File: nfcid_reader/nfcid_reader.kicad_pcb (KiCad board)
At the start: 2 copper layers, 20 parts, among them J1 BARREL_JACK, J2 ESP32_LEFT, J3 ESP32_RIGHT, J4 PN532, Q1 Q_PMOS_GSD, U1 MCP73832-2-OT, U2 LF33_TO220

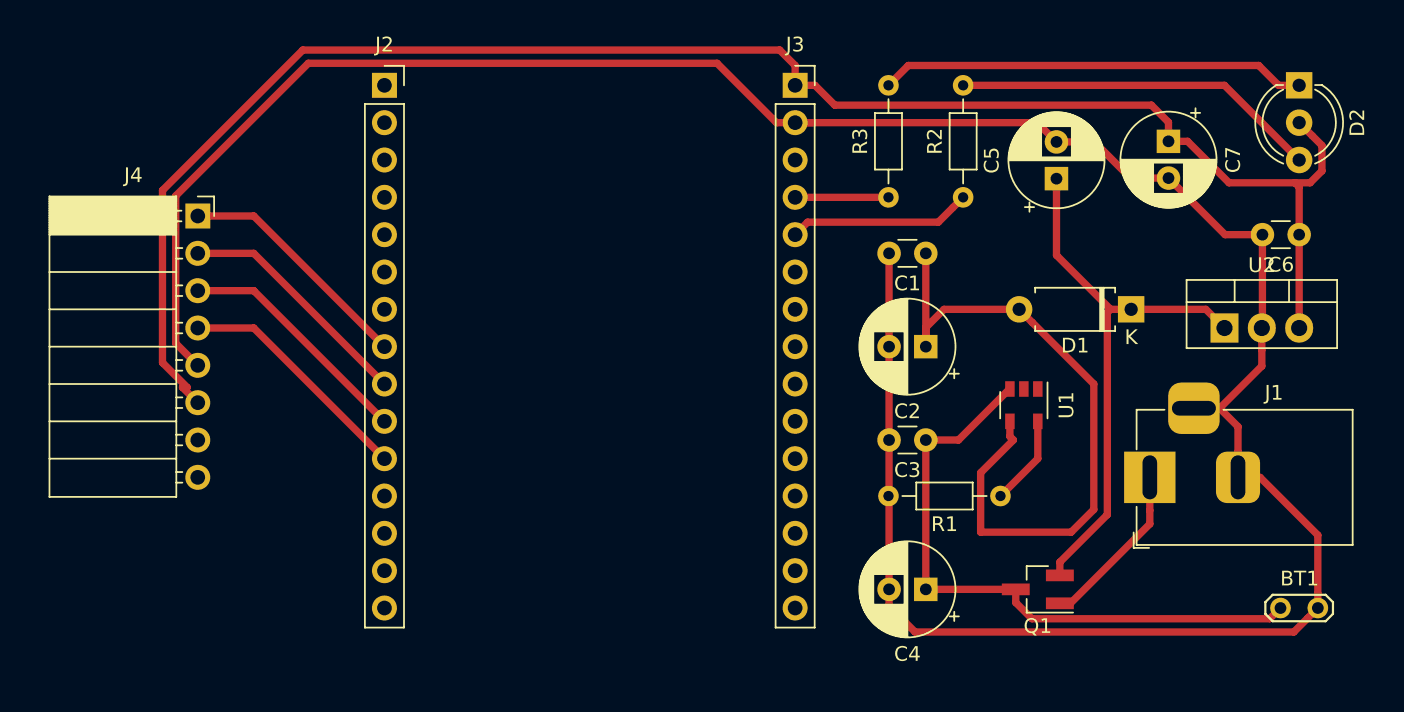
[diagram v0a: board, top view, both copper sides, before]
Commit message: Fixed thick track, ESP orentation. Added bridge, edge cuts.
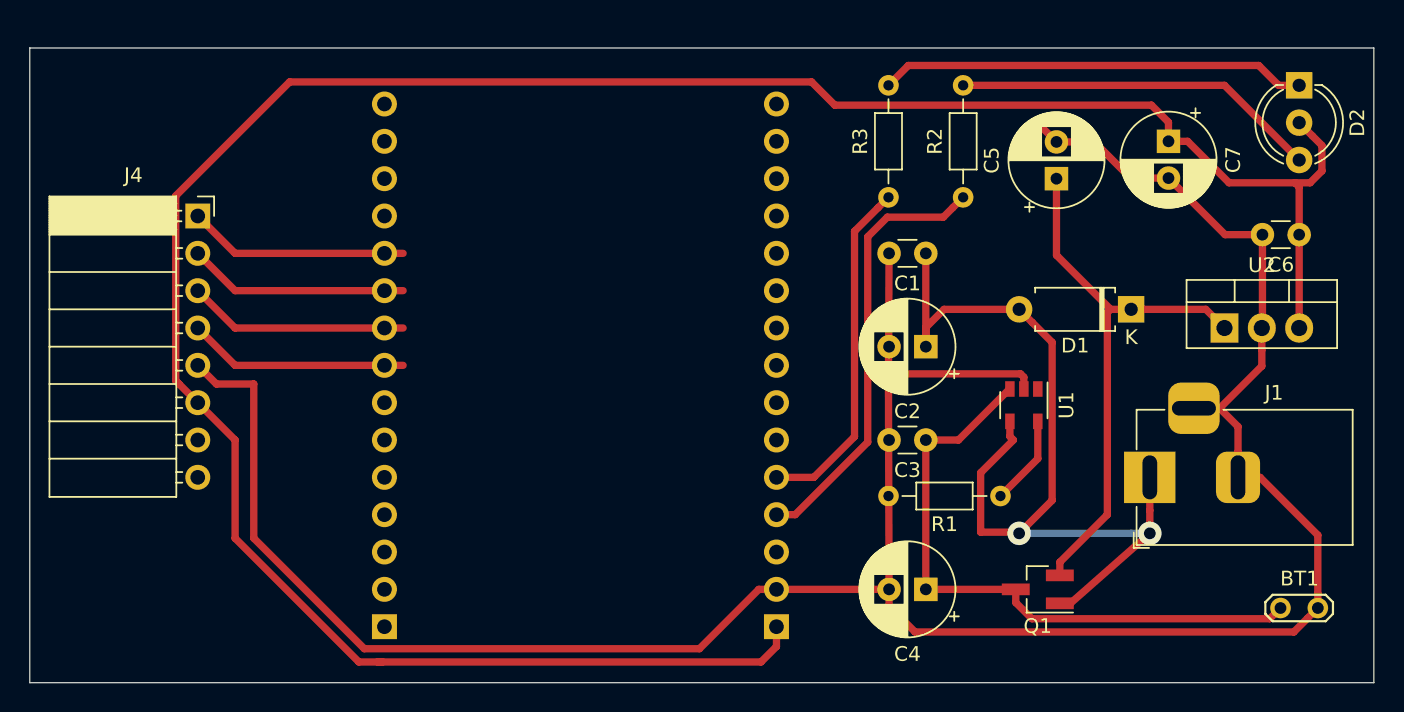
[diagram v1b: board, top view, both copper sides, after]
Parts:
- J2, J3: moved to B.Cu
- moved J3 36.9 mm to (81.3, 124.5)
- moved J2 36.8 mm to (54.6, 124.5)
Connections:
- J2 pad 10: SPI_MOSI -> SPI_MISO
- J2 pad 11: SPI_SS -> SPI_SCK
- J2 pad 8: SPI_SCK -> SPI_SS
- J2 pad 9: SPI_MISO -> SPI_MOSI
- R2 pad 1: Net-(J3-Pad5) -> Net-(J3-Pad4)
- R3 pad 1: Net-(J3-Pad4) -> Net-(J3-Pad5)
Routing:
- net +3V3: track 118.3 -> 166.4 mm
- net Net-(J3-Pad4): track 6.35 -> 29.8 mm
- net Net-(J3-Pad5): track 12.5 -> 23.7 mm
- net +5V: track 58.7 -> 63.4 mm, vias 0 -> 2
- net GND: track 182.4 -> 178.3 mm
- net SPI_MISO: track 16.4 -> 15.0 mm
- net SPI_SS: track 16.4 -> 15.0 mm
- net SPI_SCK: track 16.4 -> 15.0 mm
- net SPI_MOSI: track 16.4 -> 15.0 mm
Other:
- board outline added: 91.4 x 43.2 mm
- net class Default: clearance 0.4 -> 0.25
- rule trace_clearance: 0.4 -> 0.25

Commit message: Minor fixes.
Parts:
- J2, J3: moved to F.Cu
- moved BT1 10.6 mm to (105.0, 124.5)
- turned J2 to 180 degrees
- turned J3 to 180 degrees
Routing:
- net Net-(BT1-Pad1): track 43.1 -> 32.4 mm
- net GND: track 178.3 -> 169.1 mm
- net SPI_SS: track 15.0 -> 13.8 mm
- net SPI_SCK: track 15.0 -> 13.8 mm
- net SPI_MOSI: track 15.0 -> 13.8 mm
- net SPI_MISO: track 15.0 -> 13.8 mm
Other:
- board size 91.4 x 43.2 mm -> 83.8 x 43.2 mm
- net class Default: clearance 0.25 -> 0.4
- rule trace_clearance: 0.25 -> 0.4

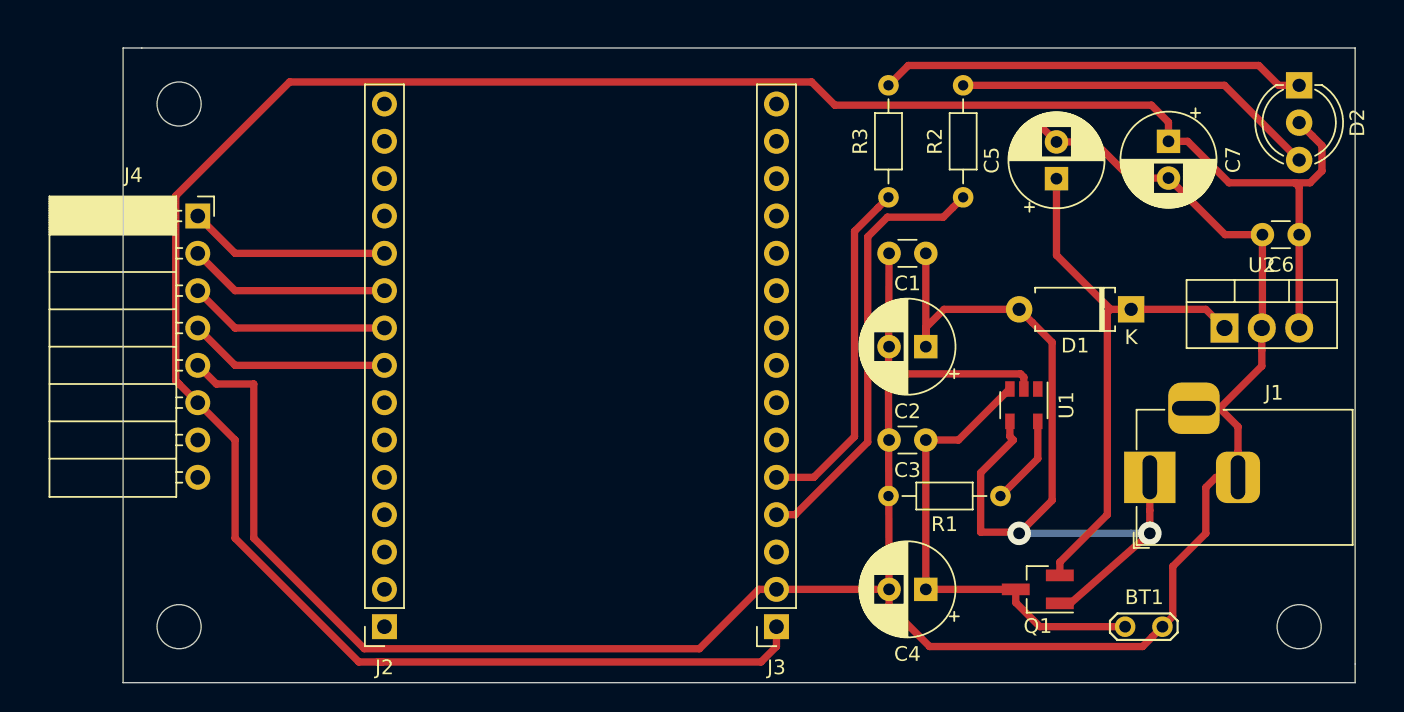
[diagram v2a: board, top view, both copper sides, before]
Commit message: RC-1: Added votage dividers. J4 fliped.
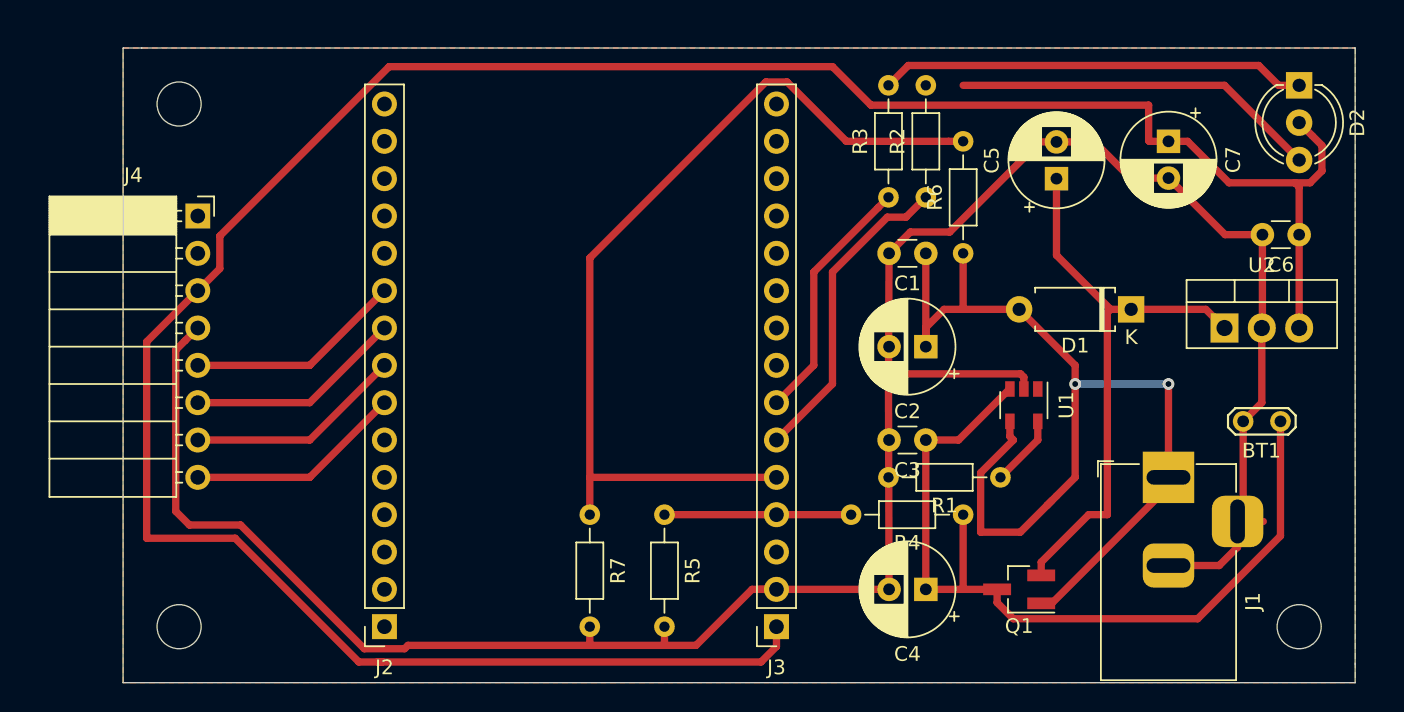
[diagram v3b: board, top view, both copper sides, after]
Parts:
- added R4: 4K7, Resistor_THT:R_Axial_DIN0204_L3.6mm_D1.6mm_P7.62mm_Horizontal, F.Cu at (94.0, 116.8)
- added R5: 1K, Resistor_THT:R_Axial_DIN0204_L3.6mm_D1.6mm_P7.62mm_Horizontal, F.Cu at (73.7, 116.8)
- added R6: 4K7, Resistor_THT:R_Axial_DIN0204_L3.6mm_D1.6mm_P7.62mm_Horizontal, F.Cu at (94.0, 99.1)
- added R7: 4K7, Resistor_THT:R_Axial_DIN0204_L3.6mm_D1.6mm_P7.62mm_Horizontal, F.Cu at (68.6, 116.8)
- moved BT1 17.5 mm to (115.6, 110.5), turned to 180 degrees
- moved R2 2.54 mm to (91.4, 95.2)
- moved J1 1.27 mm to (108.0, 114.3), turned to 90 degrees
- moved Q1 1.27 mm to (97.8, 121.9)
- moved R1 1.27 mm to (96.5, 114.3)
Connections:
- J2 pad 10: SPI_MISO -> SPI_SS
- J2 pad 11: SPI_SCK -> Net-(J2-Pad11)
- J2 pad 7: Net-(J2-Pad7) -> SPI_SCK
- J2 pad 8: SPI_SS -> SPI_MISO
- J3 pad 4: Net-(J3-Pad4) -> POW_BATT
- J3 pad 5: Net-(J3-Pad5) -> POW_SOUR
- J4 pad 1: SPI_SCK -> Net-(J4-Pad1)
- J4 pad 2: SPI_MISO -> Net-(J4-Pad2)
- J4 pad 3: SPI_MOSI -> +3V3
- J4 pad 4: SPI_SS -> GND
- J4 pad 5: GND -> SPI_SS
- J4 pad 6: +3V3 -> SPI_MOSI
- J4 pad 7: Net-(J4-Pad7) -> SPI_MISO
- J4 pad 8: Net-(J4-Pad8) -> SPI_SCK
- R2 pad 1: Net-(J3-Pad4) -> Net-(J3-Pad6)
- R3 pad 1: Net-(J3-Pad5) -> Net-(J3-Pad7)
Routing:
- net POW_SOUR: track 0.00 -> 62.2 mm
- net Net-(J3-Pad4): track 29.8 -> 0.00 mm
- net Net-(BT1-Pad1): track 32.4 -> 58.0 mm
- net Net-(J3-Pad5): track 23.7 -> 0.00 mm
- net Net-(J3-Pad6): track 0.00 -> 21.5 mm
- net Net-(J3-Pad7): track 0.00 -> 17.1 mm
- net POW_BATT: track 0.00 -> 12.7 mm
- net +5V: track 63.4 -> 73.6 mm
- net GND: track 169.1 -> 164.2 mm
- net +3V3: track 166.4 -> 169.8 mm
- net VCC: track 38.2 -> 39.5 mm
- net Net-(R1-Pad1): track 6.13 -> 4.86 mm
- net SPI_SS: track 13.8 -> 14.8 mm
- net SPI_MISO: track 13.8 -> 14.8 mm
- net SPI_SCK: track 13.8 -> 14.8 mm
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- added copper zone on F.Cu, net GND

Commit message: RC-2: U2 changed to SMD. LED moved.
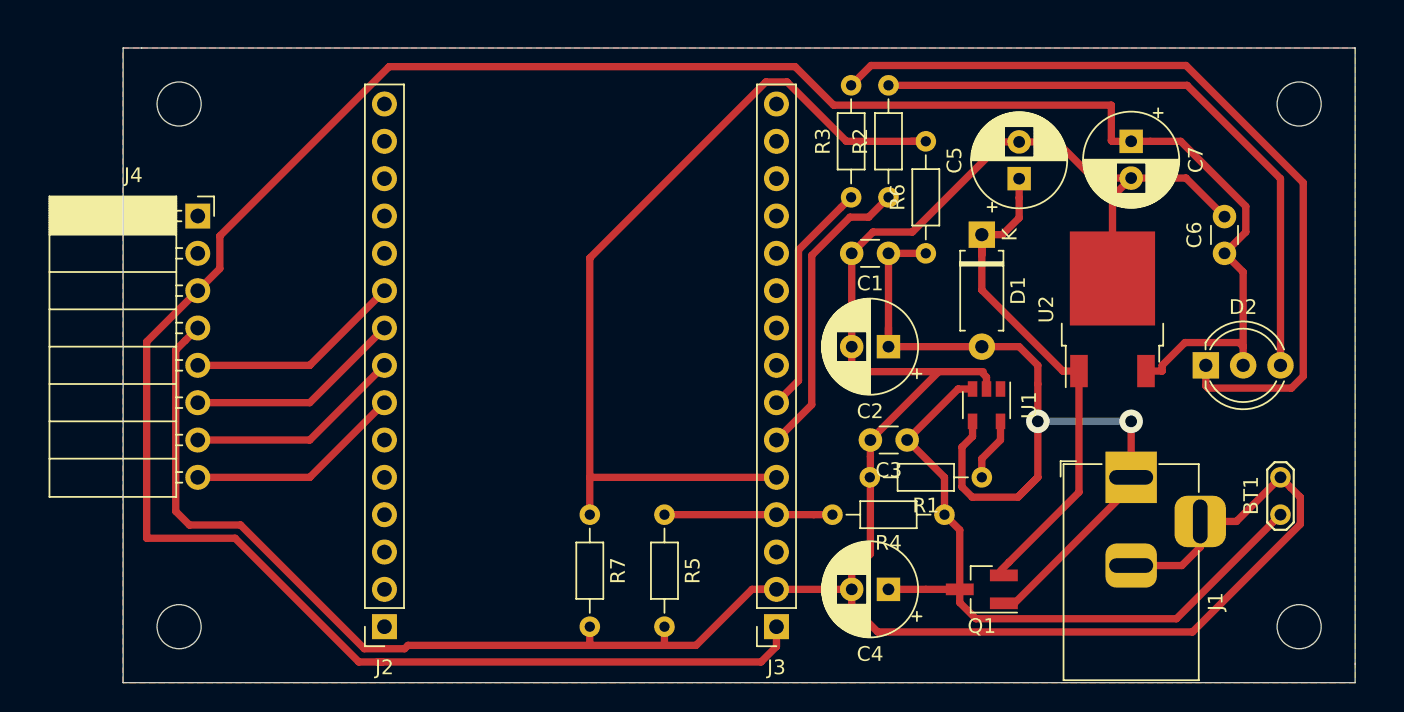
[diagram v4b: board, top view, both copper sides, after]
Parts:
- U2: footprint Package_TO_SOT_THT:TO-220-3_Vertical -> Package_TO_SOT_SMD:TO-252-2
- moved D2 20.1 mm to (110.5, 106.7), turned to 0 degrees
- moved D1 11.4 mm to (95.2, 97.8), turned to 270 degrees
- moved U2 7.73 mm to (104.1, 102.9), turned to 90 degrees
- moved BT1 6.35 mm to (115.6, 116.8), turned to 90 degrees
- moved C6 5.24 mm to (111.8, 99.1), turned to 90 degrees
- moved C7 2.54 mm to (105.4, 91.4)
- moved J1 2.54 mm to (105.4, 114.3)
- moved Q1 2.54 mm to (95.2, 121.9)
- moved R3 2.54 mm to (86.4, 95.2)
- moved R6 2.54 mm to (91.4, 99.1)
- moved U1 2.54 mm to (95.6, 109.4)
- moved C1 2.54 mm to (88.9, 99.1)
- moved C2 2.54 mm to (88.9, 105.4)
- moved C4 2.54 mm to (88.9, 121.9)
- moved C5 2.54 mm to (97.8, 94.0)
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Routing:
- net GND: track 164.2 -> 194.8 mm
- net Net-(D2-Pad1): track 29.1 -> 56.2 mm
- net Net-(D2-Pad3): track 25.0 -> 42.0 mm
- net +5V: track 73.6 -> 63.8 mm
- net Net-(BT1-Pad1): track 58.0 -> 49.1 mm
- net VCC: track 39.5 -> 35.5 mm
- net POW_SOUR: track 62.2 -> 60.6 mm
- net POW_BATT: track 12.7 -> 11.4 mm
- net Net-(J3-Pad7): track 17.1 -> 16.1 mm
- net Net-(J3-Pad6): track 21.5 -> 20.4 mm
- net +3V3: track 169.8 -> 170.7 mm
- net Net-(R1-Pad1): track 4.86 -> 4.34 mm
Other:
- outline, holes or cut-outs redrawn

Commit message: RC-3: Tracks moved to back. SMDs fliped.
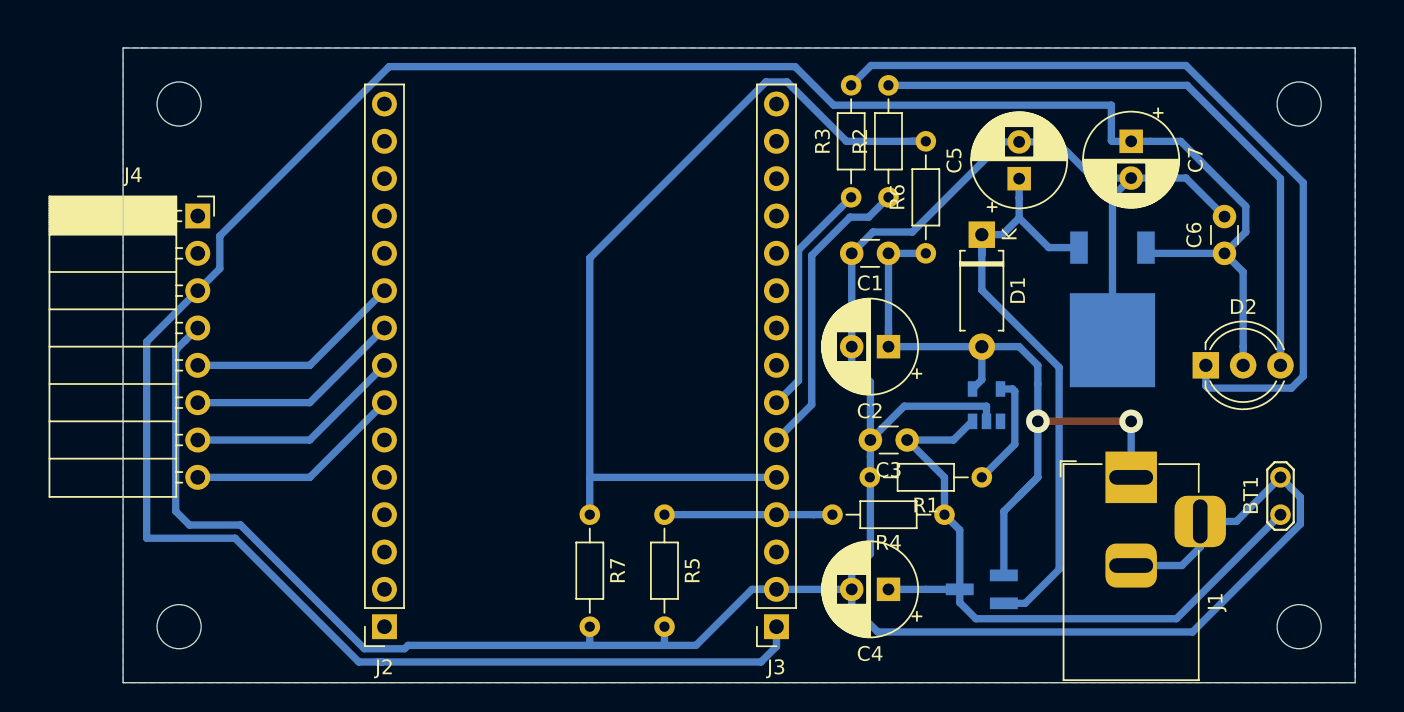
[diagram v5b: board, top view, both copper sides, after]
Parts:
- Q1, U1, U2: moved to B.Cu
- turned U1 to 90 degrees
- turned U2 to 270 degrees
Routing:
- net +5V: track 63.8 -> 51.8 mm
- net VCC: track 35.5 -> 42.4 mm
- net Net-(R1-Pad1): track 4.34 -> 7.83 mm
- net GND: track 194.8 -> 197.7 mm
- net +3V3: track 170.7 -> 168.4 mm
- net Net-(BT1-Pad1): track 49.1 -> 48.2 mm
- added copper zone on B.Cu, net GND
- removed copper zone on F.Cu, net GND

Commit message: RC4: Fixed wrong ADC pin connection.
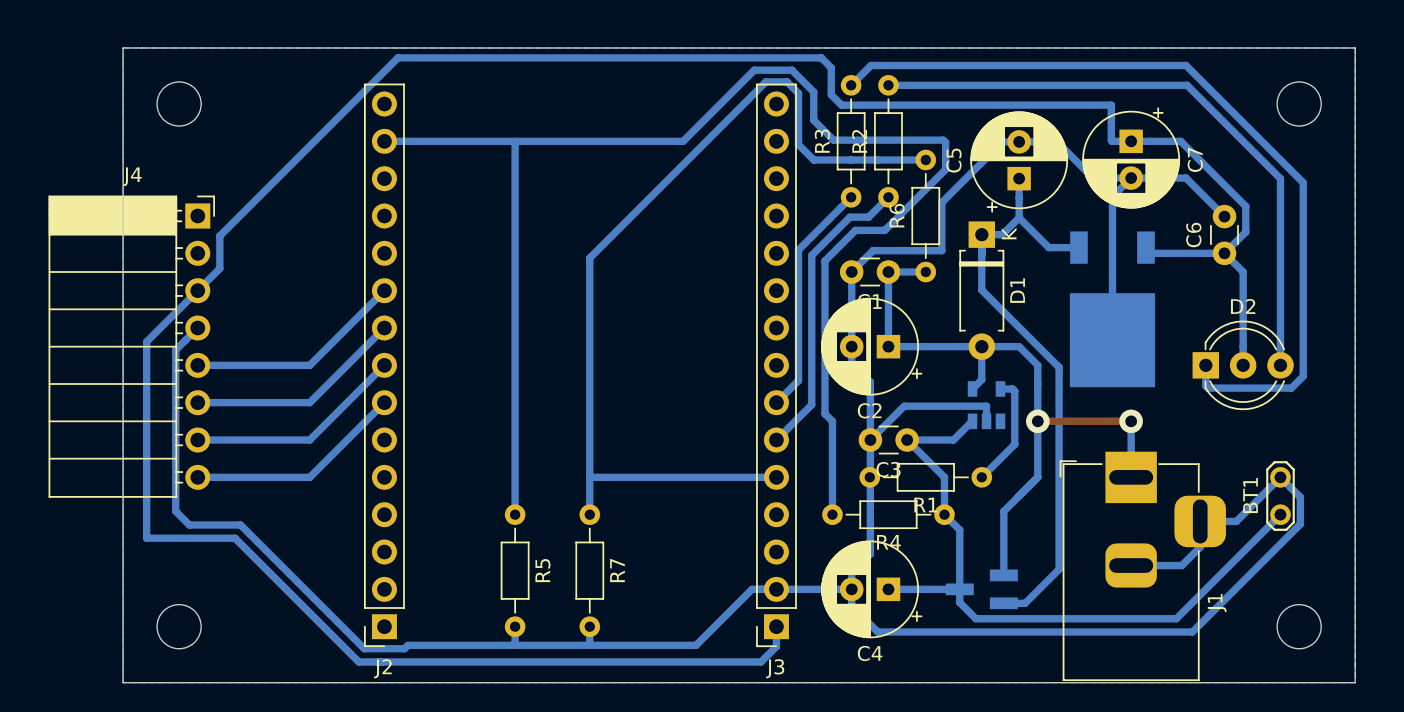
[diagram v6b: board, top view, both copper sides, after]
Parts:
- moved R5 10.2 mm to (63.5, 116.8)
- moved C1 1.27 mm to (88.9, 100.3)
- moved R6 1.27 mm to (91.4, 100.3)
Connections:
- J2 pad 14: Net-(J2-Pad14) -> POW_BATT
- J3 pad 4: POW_BATT -> Net-(J3-Pad4)
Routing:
- net POW_BATT: track 11.4 -> 98.8 mm
- net +5V: track 51.8 -> 49.3 mm
- net POW_SOUR: track 60.6 -> 62.2 mm
- net +3V3: track 168.4 -> 170.0 mm
- net GND: track 197.7 -> 198.9 mm
